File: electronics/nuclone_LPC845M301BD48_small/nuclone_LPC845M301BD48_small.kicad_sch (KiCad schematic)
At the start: 39 parts, among them J1 JTAG_2X05, J2 TYPE-C-31-M-12, J3 nuclone_small_left, J4 nuclone_small_right, SW1 RESET, SW2 Bootloader, U1 MCP1702-MB, U2 TPESD0504C6

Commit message: schematic further added
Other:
- sheet microcontroller ports: added BOOT_RX, BOOT_TX; removed none
- moved on the sheet: C5, R8, R9, SW2

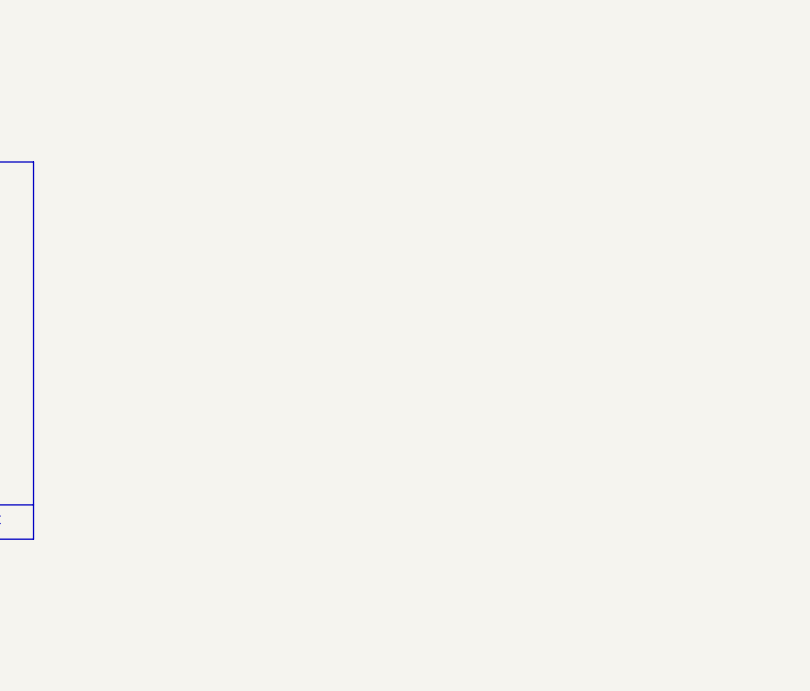
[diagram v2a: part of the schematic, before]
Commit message: added usb to serial converter in schematic and placed on PCB
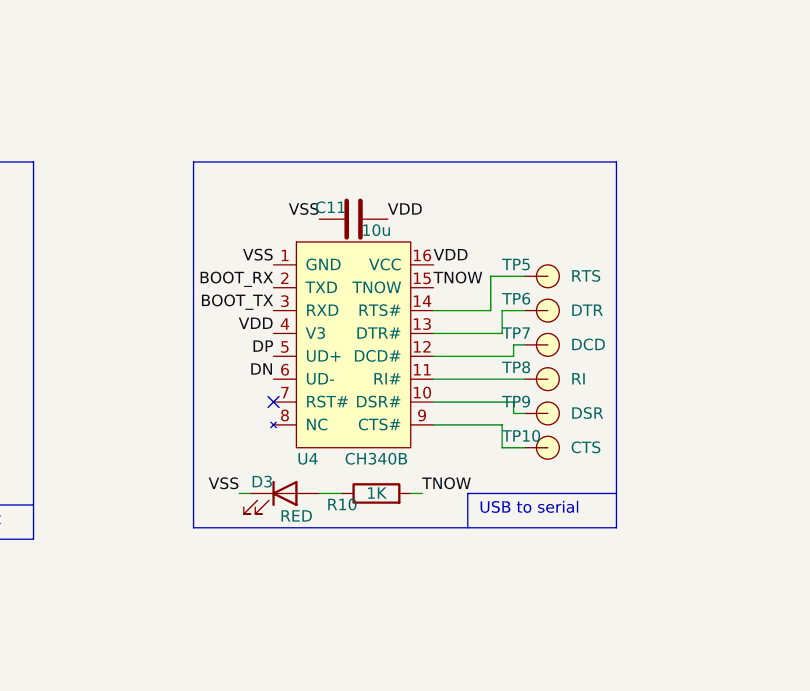
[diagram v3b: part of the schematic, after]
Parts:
- added C11: 10u, SquantorCapacitor:C_0603, symbol Device:C
- added D3: RED, SquantorDiodes:LED_0603_hand, symbol Device:LED
- added R10: 1K, SquantorResistor:R_0603_hand, symbol Device:R
- added TP10: CTS, SquantorTestPoints:TestPoint_hole_H05R10, symbol SquantorProto:testpad
- added TP5: RTS, SquantorTestPoints:TestPoint_hole_H05R10, symbol SquantorProto:testpad
- added TP6: DTR, SquantorTestPoints:TestPoint_hole_H05R10, symbol SquantorProto:testpad
- added TP7: DCD, SquantorTestPoints:TestPoint_hole_H05R10, symbol SquantorProto:testpad
- added TP8: RI, SquantorTestPoints:TestPoint_hole_H05R10, symbol SquantorProto:testpad
- added TP9: DSR, SquantorTestPoints:TestPoint_hole_H05R10, symbol SquantorProto:testpad
- added U4: CH340B, Package_SO:SO-16_3.9x9.9mm_P1.27mm, symbol SquantorWCH:CH340B
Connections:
- net BOOT_RX: now also U4.2 (TXD)
- net BOOT_TX: now also U4.3 (RXD)
- net DN: now also U4.6 (UD-)
- net DP: now also U4.5 (UD+)
- net VDD: now also C11.1, U4.16 (VCC), U4.4 (V3)
- net VSS: now also C11.2, D3.1 (K), U4.1 (GND)
- new net: TP10.1, U4.9 (CTS#)
- new net: TP5.1, U4.14 (RTS#)
- new net: TP9.1, U4.10 (DSR#)
- new net: TP8.1, U4.11 (RI#)
- new net: TP7.1, U4.12 (DCD#)
- new net: TP6.1, U4.13 (DTR#)
- new net: D3.2 (A), R10.1
- new net TNOW: R10.2, U4.15 (TNOW)
- no-connect marks 4 -> 5
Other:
- note added: "USB to serial"

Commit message: placing, routing and silk placement completed
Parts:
- U4: footprint Package_SO:SO-16_3.9x9.9mm_P1.27mm -> SquantorIC:SOIC-16_3.9x9.9mm_P1.27mm
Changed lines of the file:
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@@
       (effects (font (size 1.27 1.27)))
     )
-    (property "Footprint" "Package_SO:SO-16_3.9x9.9mm_P1.27mm" (at 120.65 99.06 0)
+    (property "Footprint" "SquantorIC:SOIC-16_3.9x9.9mm_P1.27mm" (at 120.65 99.06 0)
       (effects (font (size 1.27 1.27)) hide)
     )

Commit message: small updates
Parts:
- N4: value NuClone Small template V1.5.1 -> NuClone LPC84X PQFP48
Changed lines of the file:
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@@
       (effects (font (size 1.524 1.524)) (justify left))
     )
-    (property "Value" "NuClone Small template V1.5.1" (at 20.32 170.18 0)
+    (property "Value" "NuClone LPC84X PQFP48" (at 20.32 170.18 0)
       (effects (font (size 1.524 1.524)) (justify left))
     )

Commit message: prepped for production with updated versionnumbers and some minor changes
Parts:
- N2: value V20240606 -> V20240712
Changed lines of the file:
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@@
       (effects (font (size 1.524 1.524)) (justify left))
     )
-    (property "Value" "V20240606" (at 17.78 182.88 0)
+    (property "Value" "V20240712" (at 17.78 182.88 0)
       (effects (font (size 1.524 1.524)) (justify left))
     )
